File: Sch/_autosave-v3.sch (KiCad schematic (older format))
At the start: 8 parts

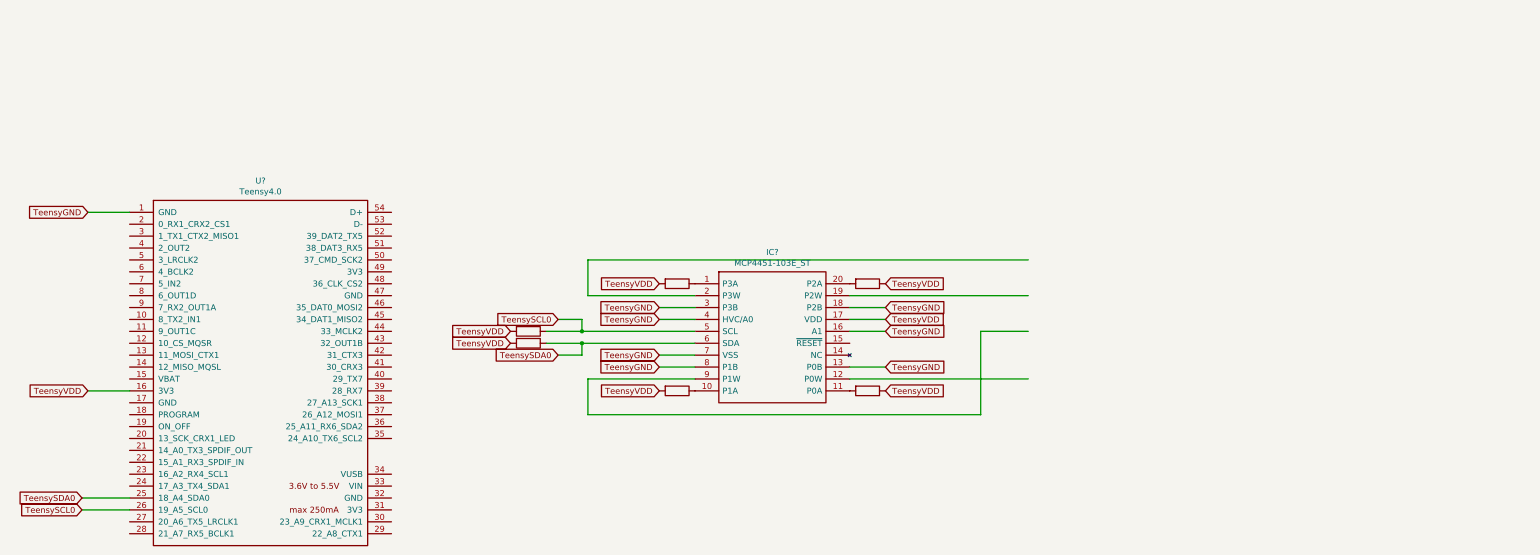
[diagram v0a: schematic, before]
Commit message: First version of first module
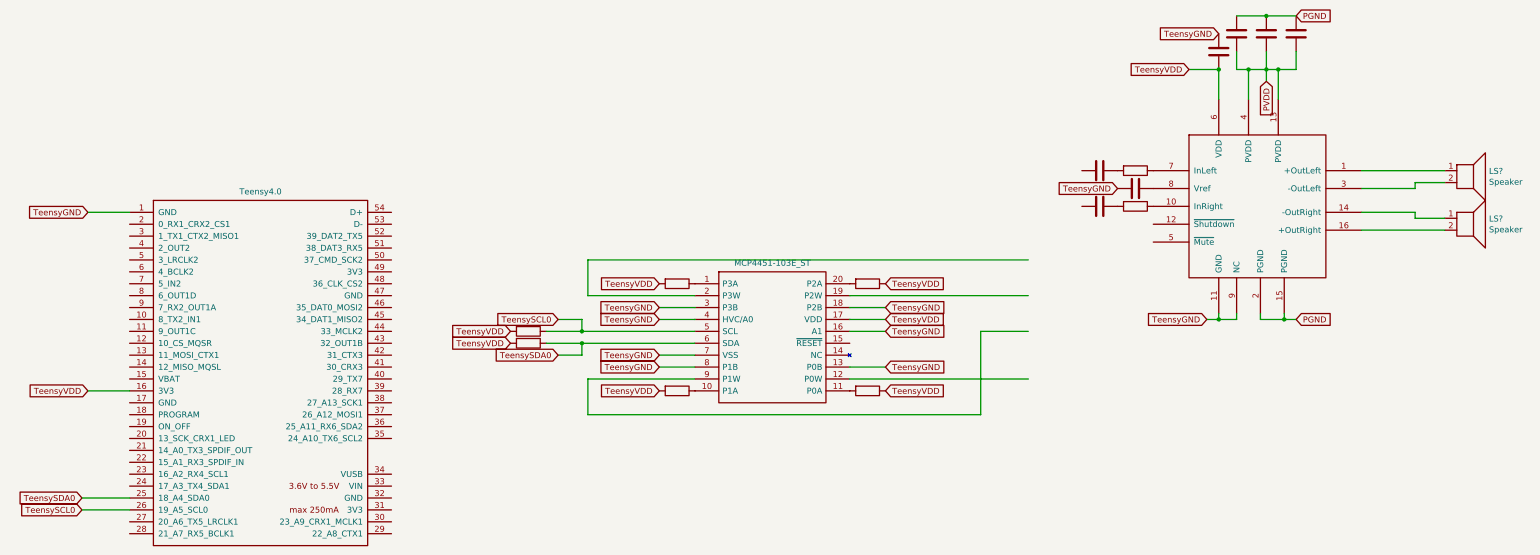
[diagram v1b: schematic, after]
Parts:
- added C?: 0.1uF, symbol Device:C
- added C? (x2): 0.47uF, symbol Device:C
- added C? (x3): 1uF, symbol Device:C
- added C?: 470uF, symbol Device:C
- added LS? (x2): Speaker, symbol Device:Speaker
- added R? (x2): 10000, symbol Device:R
- added U?: PAM8403, symbol pam8403:PAM8403
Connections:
- net labels added: PGND, PVDD
- wire segments 30 -> 60
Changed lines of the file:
@@
 U 1 1 609956D3
 P 2050 2500
-F 0 "U?" H 2050 4115 50  0000 C CNN
+F 0 "U?" H 2050 4115 50  0001 C CNN
 F 1 "Teensy4.0" H 2050 4024 50  0000 C CNN
 F 2 "" H 1650 2700 50  0001 C CNN
@@
 U 1 1 609994CF
 P 5700 1750
-F 0 "IC?" H 6350 2015 50  0000 C CNN
+F 0 "IC?" H 6350 2015 50  0001 C CNN
 F 1 "MCP4451-103E_ST" H 6350 1924 50  0000 C CNN
 F 2 "SOP65P640X120-20N" H 6850 1850 50  0001 L CNN
@@
 Wire Wire Line
 	8100 2150 8100 2850
+$Comp
+L pam8403:PAM8403 U?
+U 1 1 609BDBAE
+P 10350 1050
+F 0 "U?" H 10425 2103 60  0001 C CNN
+F 1 "PAM8403" H 10425 1997 60  0001 C CNN
+F 2 "" H 10350 1050 60  0000 C CNN
+F 3 "" H 10350 1050 60  0000 C CNN
+	1    10350 1050
+	1    0    0    -1
+$EndComp
+Text GLabel 10750 2050 2    50   Input ~ 0
+PGND
+Wire Wire Line
+	10650 2000 10650 2050
+Wire Wire Line
+	10650 2050 10750 2050
+Wire Wire Line
+	10450 2000 10450 2050
+$Comp
+L Device:Speaker LS?
+U 1 1 609A3FD9
+P 12200 800
+F 0 "LS?" H 12370 796 50  0000 L CNN
+F 1 "Speaker" H 12370 705 50  0000 L CNN
+F 2 "" H 12200 600 50  0001 C CNN
+F 3 "~" H 12190 750 50  0001 C CNN
+	1    12200 800
+	1    0    0    -1
+$EndComp
+$Comp
+L Device:Speaker LS?
+U 1 1 609A64B9
+P 12200 1200
+F 0 "LS?" H 12370 1196 50  0000 L CNN
+F 1 "Speaker" H 12370 1105 50  0000 L CNN
+F 2 "" H 12200 1000 50  0001 C CNN
+F 3 "~" H 12190 1150 50  0001 C CNN
+	1    12200 1200
+	1    0    0    -1
+$EndComp
+Wire Wire Line
+	11300 800  12000 800
+Wire Wire Line
+	11300 950  11750 950
+Wire Wire Line
+	11750 950  11750 900
+Wire Wire Line
+	11750 900  12000 900
+Wire Wire Line
+	11300 1150 11750 1150
+Wire Wire Line
+	11750 1150 11750 1200
+Wire Wire Line
+	11750 1200 12000 1200
+Wire Wire Line
+	11300 1300 12000 1300
+$Comp
+L Device:R R?
+U 1 1 609AC19B
+P 9400 800
+F 0 "R?" V 9193 800 50  0001 C CNN
+F 1 "10000" V 9284 800 50  0001 C CNN
+F 2 "" V 9330 800 50  0001 C CNN
+F 3 "~" H 9400 800 50  0001 C CNN
+	1    9400 800
+	0    1    1    0
+$EndComp
+$Comp
+L Device:R R?
+U 1 1 609ACC76
+P 9400 1100
+F 0 "R?" V 9193 1100 50  0001 C CNN
+F 1 "10000" V 9284 1100 50  0001 C CNN
+F 2 "" V 9330 1100 50  0001 C CNN
+F 3 "~" H 9400 1100 50  0001 C CNN
+	1    9400 1100
+	0    1    1    0
+$EndComp
+$Comp
+L Device:C C?
+U 1 1 609ADA18
+P 9400 950
+F 0 "C?" V 9148 950 50  0001 C CNN
+F 1 "0.1uF" V 9239 950 50  0001 C CNN
+F 2 "" H 9438 800 50  0001 C CNN
+F 3 "~" H 9400 950 50  0001 C CNN
+	1    9400 950
+	0    1    1    0
+$EndComp
+$Comp
+L Device:C C?
+U 1 1 609AF85E
+P 9100 800
+F 0 "C?" V 8848 800 50  0001 C CNN
+F 1 "0.47uF" V 8939 800 50  0001 C CNN
+F 2 "" H 9138 650 50  0001 C CNN
+F 3 "~" H 9100 800 50  0001 C CNN
+	1    9100 800
+	0    1    1    0
+$EndComp
+$Comp
+L Device:C C?
+U 1 1 609B0307
+P 9100 1100
+F 0 "C?" V 8848 1100 50  0001 C CNN
+F 1 "0.47uF" V 8939 1100 50  0001 C CNN
+F 2 "" H 9138 950 50  0001 C CNN
+F 3 "~" H 9100 1100 50  0001 C CNN
+	1    9100 1100
+	0    1    1    0
+$EndComp
+Text GLabel 9850 -50  0    50   Input ~ 0
+TeensyVDD
+$Comp
+L Device:C C?
+U 1 1 609B5C80
+P 10750 -350
+F 0 "C?" V 10498 -350 50  0001 C CNN
+F 1 "1uF" V 10589 -350 50  0001 C CNN
+F 2 "" H 10788 -500 50  0001 C CNN
+F 3 "~" H 10750 -350 50  0001 C CNN
+	1    10750 -350
+	1    0    0    -1
+$EndComp
+$Comp
+L Device:C C?
+U 1 1 609BFFCB
+P 10250 -350
+F 0 "C?" V 9998 -350 50  0001 C CNN
+F 1 "1uF" V 10089 -350 50  0001 C CNN
+F 2 "" H 10288 -500 50  0001 C CNN
+F 3 "~" H 10250 -350 50  0001 C CNN
+	1    10250 -350
+	1    0    0    -1
+$EndComp
+$Comp
+L Device:C C?
+U 1 1 609C0D09
+P 10500 -350
+F 0 "C?" V 10248 -350 50  0001 C CNN
+F 1 "470uF" V 10339 -350 50  0001 C CNN
+F 2 "" H 10538 -500 50  0001 C CNN
+F 3 "~" H 10500 -350 50  0001 C CNN
+	1    10500 -350
+	1    0    0    -1
+$EndComp
+Text GLabel 10750 -500 2    50   Input ~ 0
+PGND
+Wire Wire Line
+	10250 -200 10250 -50
+Wire Wire Line
+	10250 -50  10350 -50
+Wire Wire Line
+	10500 -200 10500 -50
+Wire Wire Line
+	10500 -50  10600 -50
+Wire Wire Line
+	10750 -50  10750 -200
+Connection ~ 10500 -50
+Wire Wire Line
+	10350 200  10350 -50
+Connection ~ 10350 -50
+Wire Wire Line
+	10350 -50  10500 -50
+Wire Wire Line
+	10600 200  10600 -50
+Connection ~ 10600 -50
+Wire Wire Line
+	10600 -50  10750 -50
+Text GLabel 10500 50   3    50   Input ~ 0
+PVDD
+Wire Wire Line
+	10500 50   10500 -50
+Wire Wire Line
+	10100 -50  10100 200
+$Comp
+L Device:C C?
+U 1 1 609D6805
+P 10100 -200
+F 0 "C?" V 9848 -200 50  0001 C CNN
+F 1 "1uF" V 9939 -200 50  0001 C CNN
+F 2 "" H 10138 -350 50  0001 C CNN
+F 3 "~" H 10100 -200 50  0001 C CNN
+	1    10100 -200
+	1    0    0    -1
+$EndComp
+Text GLabel 10100 -350 0    50   Input ~ 0
+TeensyGND
+Text GLabel 10000 2050 0    50   Input ~ 0
+TeensyGND
+Wire Wire Line
+	10100 2000 10100 2050
+Wire Wire Line
+	10100 2050 10000 2050
+Wire Wire Line
+	10250 2000 10250 2050
+Text GLabel 9250 950  0    50   Input ~ 0
+TeensyGND
+Connection ~ 10650 2050
+Wire Wire Line
+	10450 2050 10650 2050
+Connection ~ 10100 2050
+Wire Wire Line
+	10100 2050 10250 2050
+Wire Wire Line
+	9850 -50  10100 -50
+Connection ~ 10100 -50
+Wire Wire Line
+	10250 -500 10500 -500
+Wire Wire Line
+	10500 -500 10750 -500
+Connection ~ 10500 -500
 $EndSCHEMATC
